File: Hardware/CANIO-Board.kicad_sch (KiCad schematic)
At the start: 0 parts

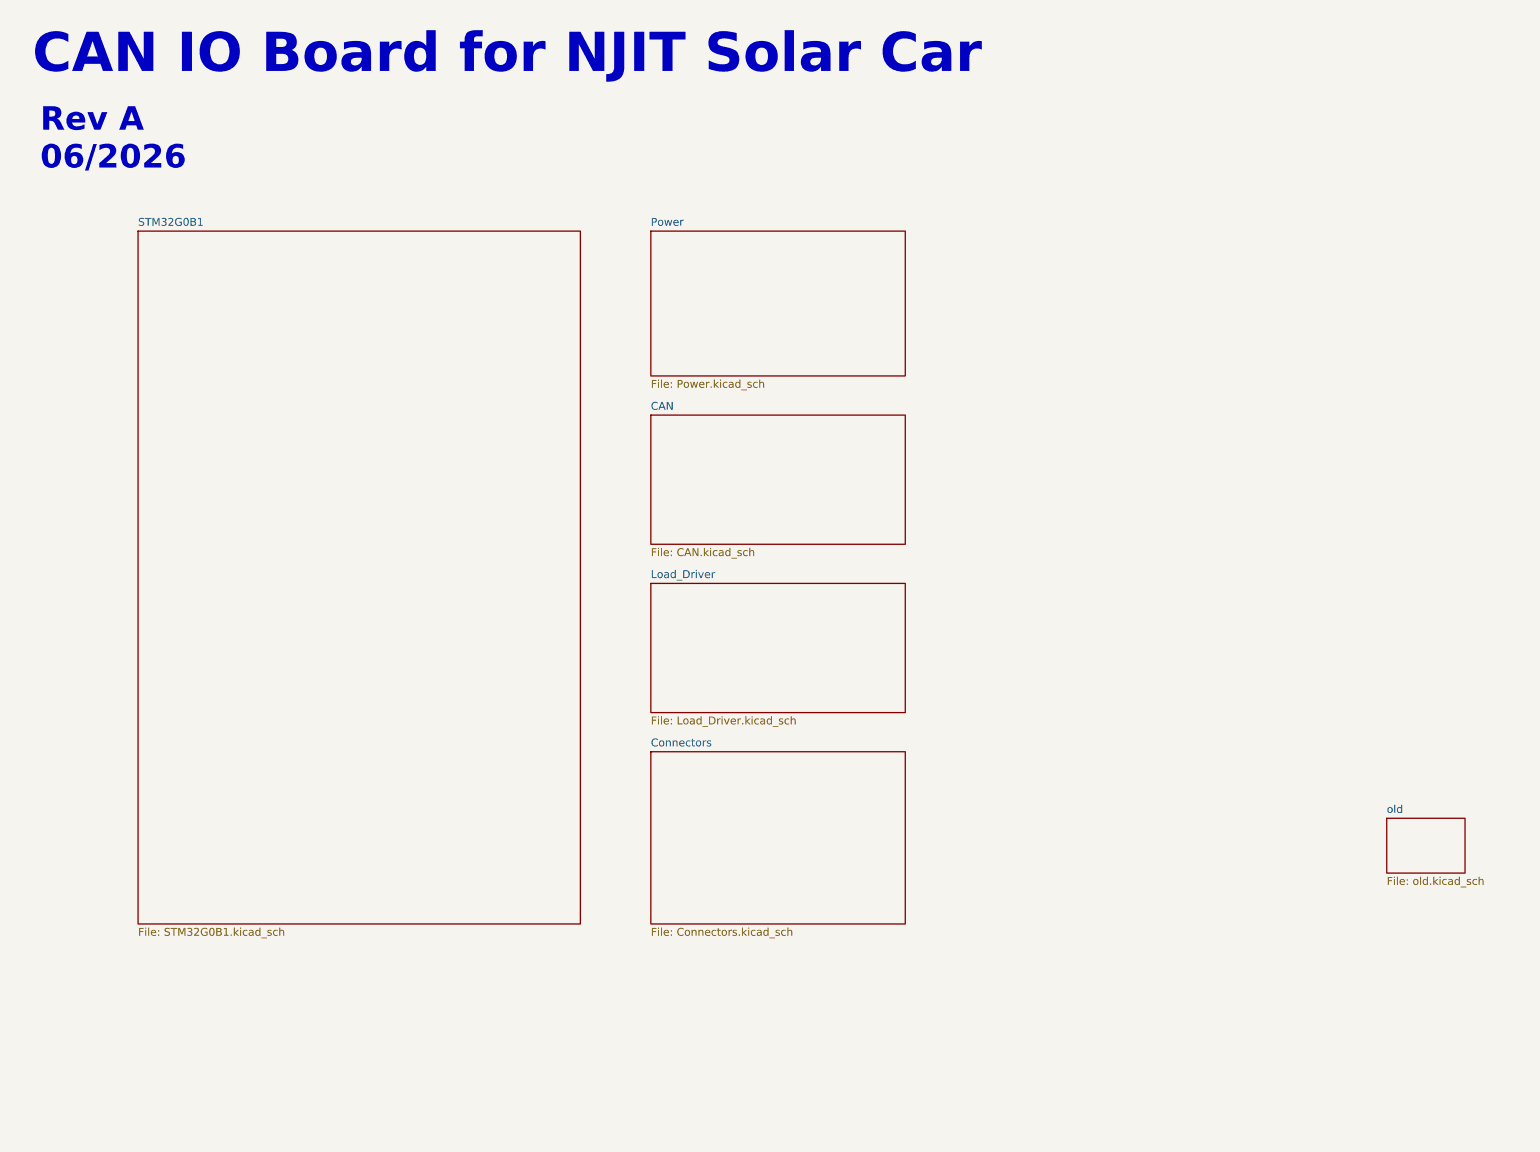
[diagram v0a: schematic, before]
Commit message: Added the power schematic
- Finished the power schematic.
- HOWEVER, there is some confusion (Arnav) about the post-supply
  filtering. Needs to be reviewed before ordering.

Co-authored-by: Nicholas Nunez <ngnunez@icloud.com>
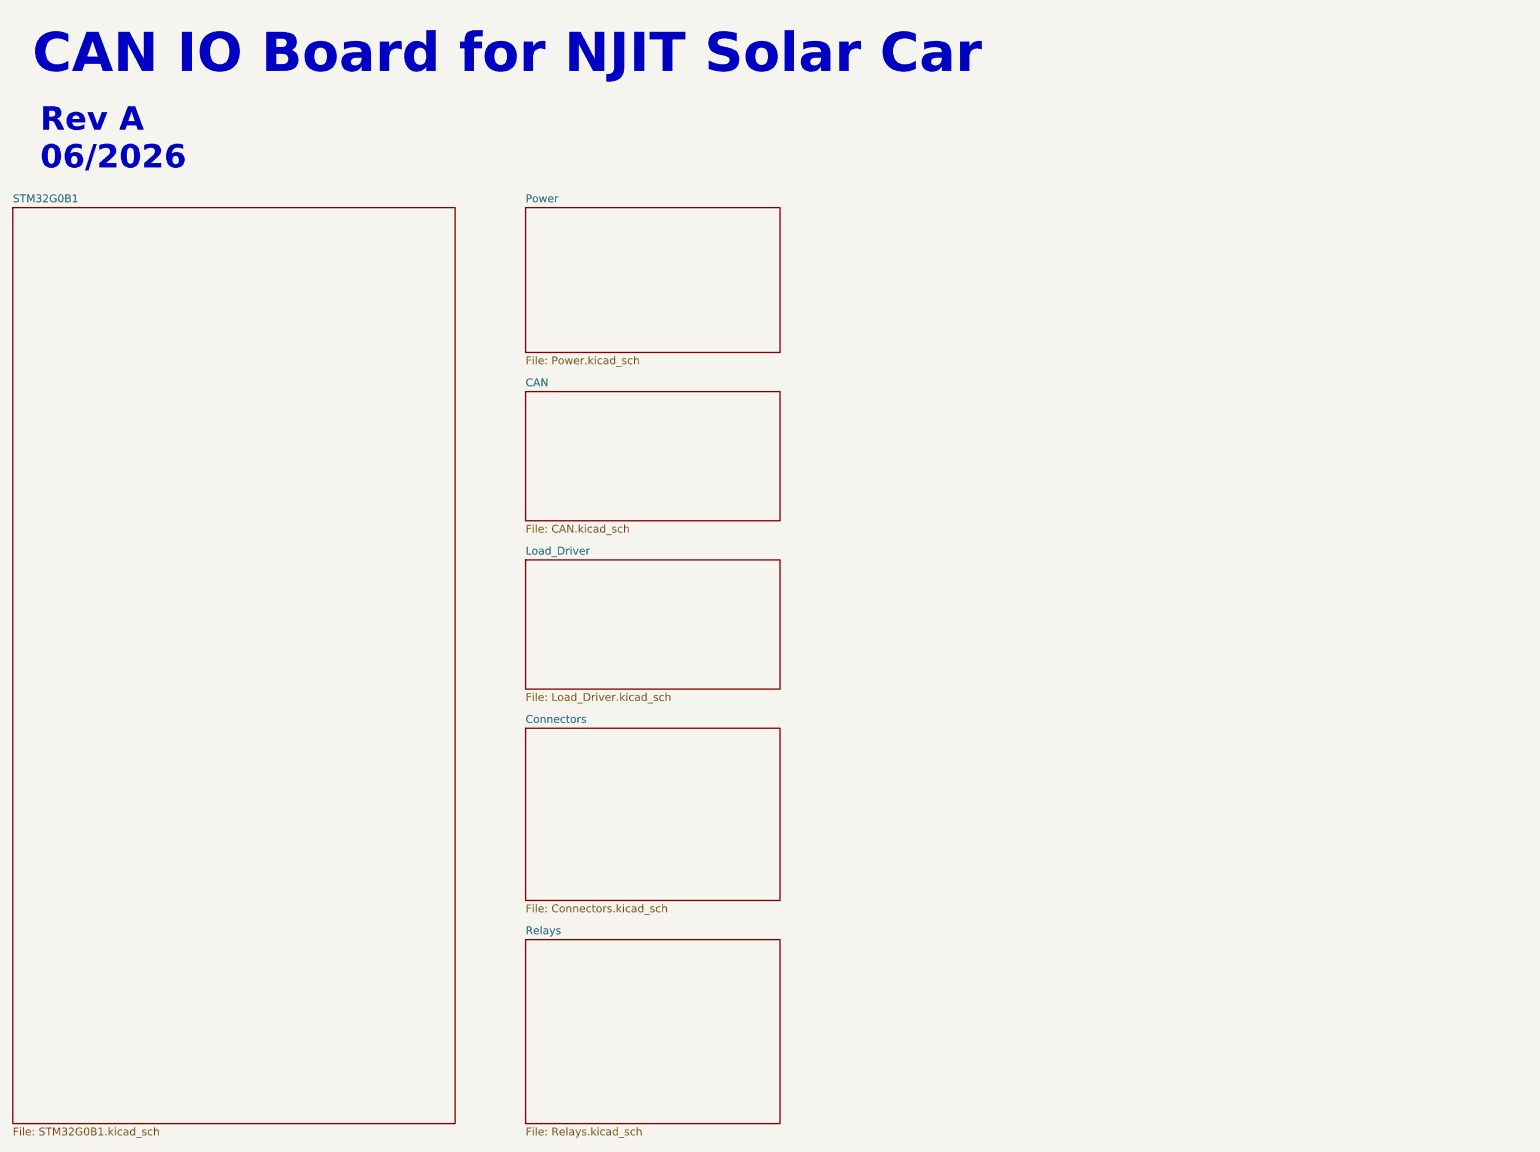
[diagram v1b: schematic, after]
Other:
- removed sheet old
- added sheet Relays (Relays.kicad_sch)
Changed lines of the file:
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@@
 	)
 	(sheet
-		(at 120.65 112.395)
+		(at 100.33 108.585)
 		(size 41.275 20.955)
 		(exclude_from_sim no)
@@
 		)
 		(property "Sheetname" "Load_Driver"
-			(at 120.65 111.6834 0)
+			(at 100.33 107.8734 0)
 			(effects
 				(font
@@
 		)
 		(property "Sheetfile" "Load_Driver.kicad_sch"
-			(at 120.65 133.9346 0)
+			(at 100.33 130.1246 0)
 			(effects
 				(font
@@
 	)
 	(sheet
-		(at 37.465 55.245)
-		(size 71.755 112.395)
+		(at 17.145 51.435)
+		(size 71.755 148.59)
 		(exclude_from_sim no)
 		(in_bom yes)
@@
 		)
 		(property "Sheetname" "STM32G0B1"
-			(at 37.465 54.5334 0)
+			(at 17.145 50.7234 0)
 			(effects
 				(font
@@
 		)
 		(property "Sheetfile" "STM32G0B1.kicad_sch"
-			(at 37.465 168.2246 0)
+			(at 17.145 200.6096 0)
 			(effects
 				(font
@@
 	)
 	(sheet
-		(at 120.65 55.245)
+		(at 100.33 51.435)
 		(size 41.275 23.495)
 		(exclude_from_sim no)
@@
 		)
 		(property "Sheetname" "Power"
-			(at 120.65 54.5334 0)
+			(at 100.33 50.7234 0)
 			(effects
 				(font
@@
 		)
 		(property "Sheetfile" "Power.kicad_sch"
-			(at 120.65 79.3246 0)
+			(at 100.33 75.5146 0)
 			(effects
 				(font
@@
 	)
 	(sheet
-		(at 120.65 139.7)
+		(at 100.33 170.18)
+		(size 41.275 29.845)
+		(exclude_from_sim no)
+		(in_bom yes)
+		(on_board yes)
+		(dnp no)
+		(fields_autoplaced yes)
+		(stroke
+			(width 0.1524)
+			(type solid)
+		)
+		(fill
+			(color 202 202 255 1.0000)
+		)
+		(property "Sheetname" "Relays"
+			(at 100.33 169.4684 0)
+			(effects
+				(font
+					(size 1.27 1.27)
+				)
+				(justify left bottom)
+			)
+		)
+		(property "Sheetfile" "Relays.kicad_sch"
+			(at 100.33 200.6096 0)
+			(effects
+				(font
+					(size 1.27 1.27)
+				)
+				(justify left top)
+			)
+		)
+		(instances
+			(project "CANIO-Board"
+				(path "/a11f98b2-3b09-4cf9-8535-19e509fe91b9"
+					(page "7")
+				)
+			)
+		)
+	)
+	(sheet
+		(at 100.33 135.89)
 		(size 41.275 27.94)
 		(exclude_from_sim no)
@@
 		)
 		(property "Sheetname" "Connectors"
-			(at 120.65 138.9884 0)
+			(at 100.33 135.1784 0)
 			(effects
 				(font
@@
 		)
 		(property "Sheetfile" "Connectors.kicad_sch"
-			(at 120.65 168.2246 0)
+			(at 100.33 164.4146 0)
 			(effects
 				(font
@@
 	)
 	(sheet
-		(at 120.65 85.09)
+		(at 100.33 81.28)
 		(size 41.275 20.955)
 		(exclude_from_sim no)
@@
 		)
 		(property "Sheetname" "CAN"
-			(at 120.65 84.3784 0)
+			(at 100.33 80.5684 0)
 			(effects
 				(font
@@
 		)
 		(property "Sheetfile" "CAN.kicad_sch"
-			(at 120.65 106.6296 0)
+			(at 100.33 102.8196 0)
 			(effects
 				(font
@@
 				)
 			)
-		)
-	)
-	(sheet
-		(at 240.03 150.495)
-		(size 12.7 8.89)
-		(exclude_from_sim no)
-		(in_bom yes)
-		(on_board yes)
-		(dnp no)
-		(fields_autoplaced yes)
-		(stroke
-			(width 0.1524)
-			(type solid)
-		)
-		(fill
-			(color 202 202 255 1.0000)
-		)
-		(property "Sheetname" "old"
-			(at 240.03 149.7834 0)
-			(effects
-				(font
-					(size 1.27 1.27)
-				)
-				(justify left bottom)
-			)
-		)
-		(property "Sheetfile" "old.kicad_sch"
-			(at 240.03 159.9696 0)
-			(effects
-				(font
-					(size 1.27 1.27)
-				)
-				(justify left top)
-			)
-		)
-		(instances
-			(project "CANIO-Board"
-				(path "/a11f98b2-3b09-4cf9-8535-19e509fe91b9"
-					(page "7")
-				)
-			)
